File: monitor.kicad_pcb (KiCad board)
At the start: 4 copper layers, 35.5 x 33.7 mm, 51 parts, among them J1 USB_C_Plug, J2 USB_C_Receptacle_USB2.0_14P, J3 Display, J4 Program, J5 Boot, U1 STM32U031K8Ux, U2 TPSM365R6V3RDNR, U3 TMP117xxDRV, U4 REF5025ADGK, U5 CC6903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

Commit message: Footprint tweaks.
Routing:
- net GND: track 37.6 -> 42.0 mm
- net /DA-: track 30.2 -> 29.6 mm
- net /DA+: track 30.2 -> 29.6 mm

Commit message: Manufacturing updates
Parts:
- moved U2 0.55 mm to (113.3, 90.5)

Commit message: Robustify reset
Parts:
- added C20: 0u1, Capacitor_SMD:C_0402_1005Metric, F.Cu at (92.9, 108.6)
- added R19: 10k, Resistor_SMD:R_0603_1608Metric, B.Cu at (89.1, 114.0)
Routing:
- net /Vout: track 42.0 -> 50.0 mm, vias 6 -> 10
- net /VBus: track 32.9 -> 40.1 mm, vias 6 -> 8
- net GND: track 42.0 -> 44.8 mm, vias 43 -> 44
- net +3V3: track 237.2 -> 239.2 mm
- net Net-(J4-Pin_1): track 2.60 -> 4.60 mm

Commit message: Update monitor for actual display
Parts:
- removed R19: 10k, Resistor_SMD:R_0603_1608Metric
- H2: moved to B.Cu
- J3: footprint Parts:PinHeader_1x04_P2.54mm_Vertical -> Connector_JST:JST_EH_B4B-EH-A_1x04_P2.50mm_Vertical
- R1, R2, R7: footprint Resistor_SMD:R_0603_1608Metric -> Resistor_SMD:R_0402_1005Metric
- moved R13 8.36 mm to (101.2, 84.8)
- moved R1 8.04 mm to (98.6, 99.3), turned to 0 degrees
- moved C2 7.86 mm to (103.2, 96.6), turned to 90 degrees
- moved U5 4.52 mm to (99.9, 94.6), turned to -90 degrees
- moved R14 3.06 mm to (103.8, 84.8)
- moved R3 2.69 mm to (105.4, 91.6), turned to 0 degrees
- moved J3 2.53 mm to (96.2, 87.7), turned to 0 degrees
- moved R18 1.50 mm to (86.5, 92.2), turned to 180 degrees
- moved R17 1.26 mm to (86.5, 90.5), turned to 180 degrees
- moved D2 1.20 mm to (84.0, 92.2), turned to 0 degrees
- moved H1 1.00 mm to (84.2, 86.2)
- moved H2 1.00 mm to (115.8, 86.2), turned to 180 degrees
- moved D1 0.94 mm to (84.0, 90.5), turned to 0 degrees
- moved C9 0.32 mm to (96.0, 104.6)
- moved R2 0.30 mm to (98.6, 100.3)
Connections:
- J3 pad 1: +3V3 -> GND
- J3 pad 2: GND -> +3V3
- U5 pad 1: /Vout -> /VBus
- U5 pad 2: /Vout -> /VBus
- U5 pad 3: /VBus -> /Vout
- U5 pad 4: /VBus -> /Vout
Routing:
- net /VBus: track 40.1 -> 21.8 mm, vias 8 -> 0
- net /ISense: track 16.8 -> 7.74 mm
- net /VSense: track 13.8 -> 5.62 mm
- net /Vout: track 50.0 -> 46.6 mm
- net GND: track 44.8 -> 48.1 mm
- net /VBusFilt: track 7.13 -> 9.75 mm
- net /Red: track 26.2 -> 28.5 mm
- net Net-(J4-Pin_1): track 4.60 -> 2.60 mm
- net /PVcc: track 6.37 -> 5.16 mm, vias 2 -> 0
- net /SDA: track 40.4 -> 39.2 mm
- net Net-(D1-A): track 2.26 -> 1.20 mm
- net Net-(D2-A): track 2.21 -> 1.20 mm
- net +3V3: track 239.2 -> 239.9 mm, vias 13 -> 16
- net Earth: track 41.4 -> 40.8 mm
- removed copper zone on B.Cu, net /VBus

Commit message: Do a round of DRC and tidy-up.
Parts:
- moved R5 3.51 mm to (93.8, 84.8)
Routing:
- net /Alert: track 29.3 -> 30.0 mm

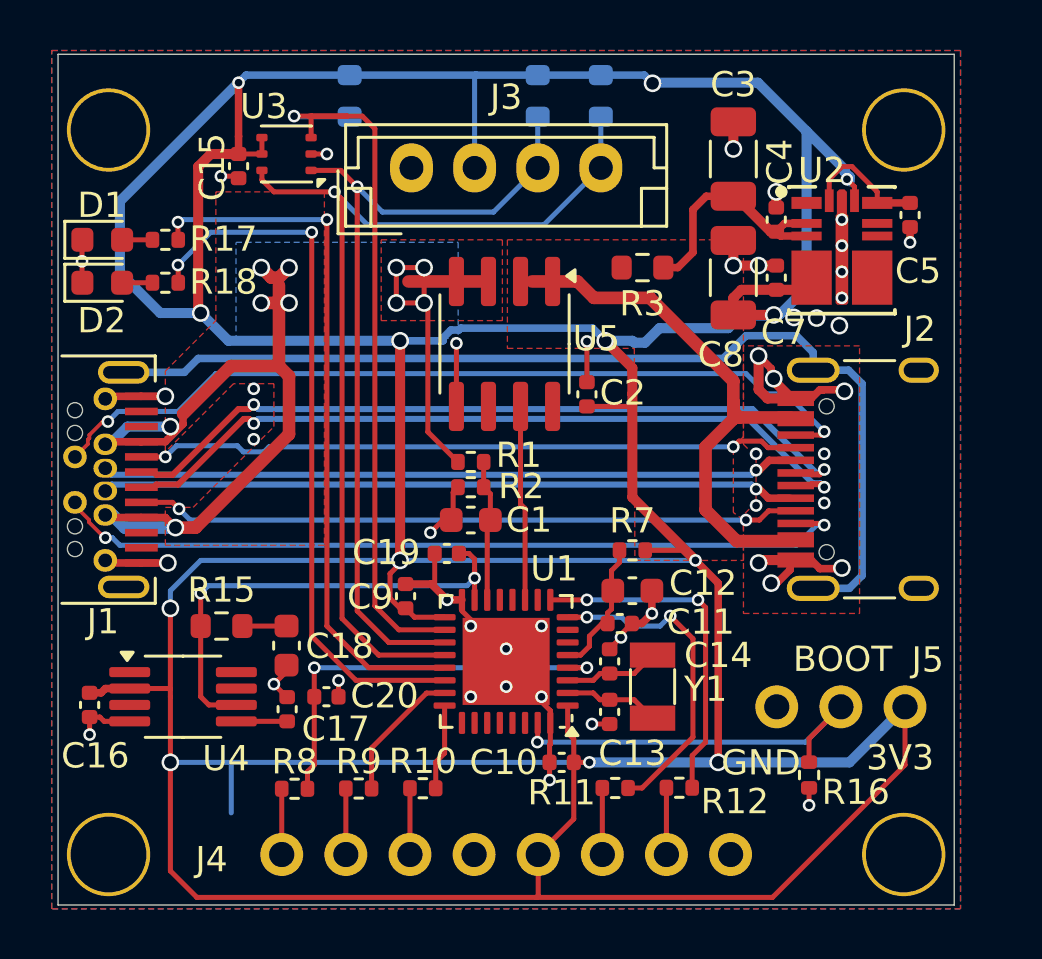
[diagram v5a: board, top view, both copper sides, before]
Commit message: Use a 2.54mm connector footprint.
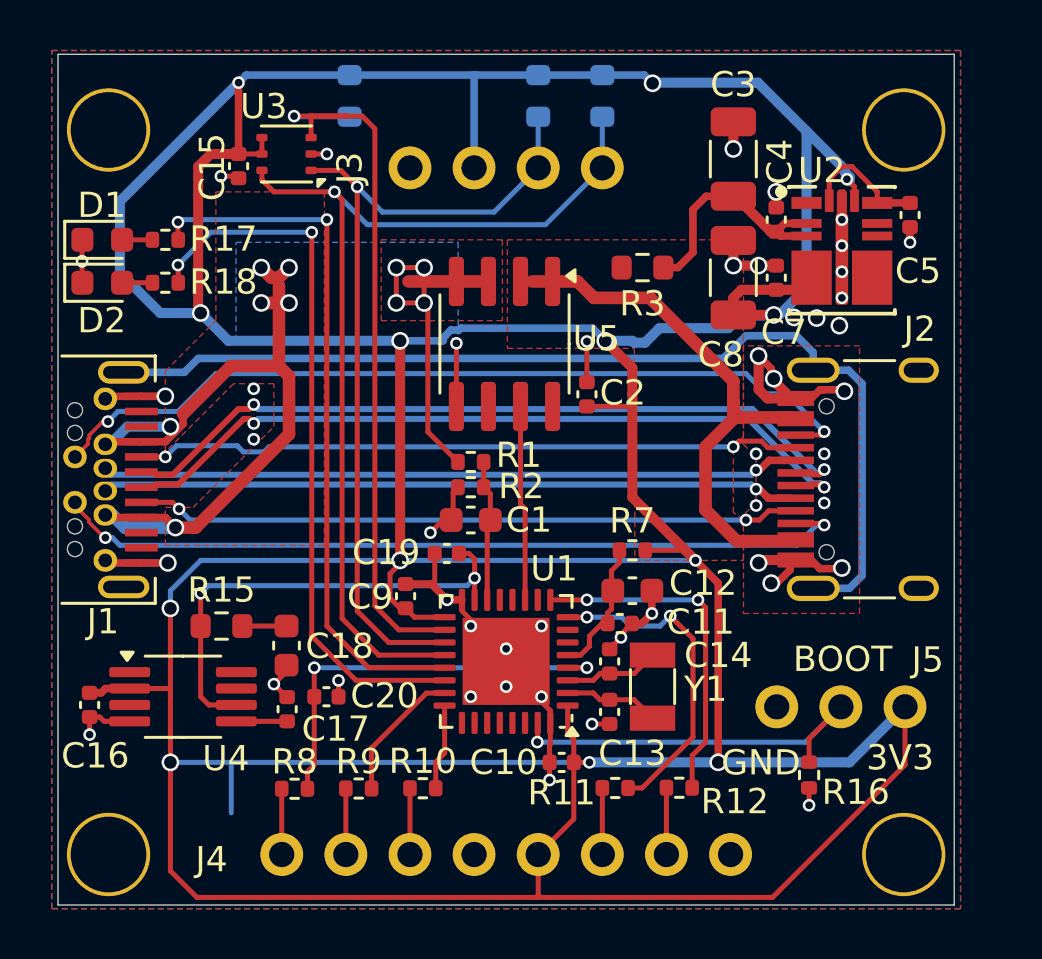
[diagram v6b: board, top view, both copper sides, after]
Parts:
- J3: footprint Connector_JST:JST_EH_B4B-EH-A_1x04_P2.50mm_Vertical -> Parts:PinHeader_1x04_P2.54mm_Vertical
- moved J3 0.06 mm to (96.2, 87.7), turned to 90 degrees
- moved R14 0.06 mm to (103.8, 84.8)

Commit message: Filter ADC input.
Tweak other capacitors.
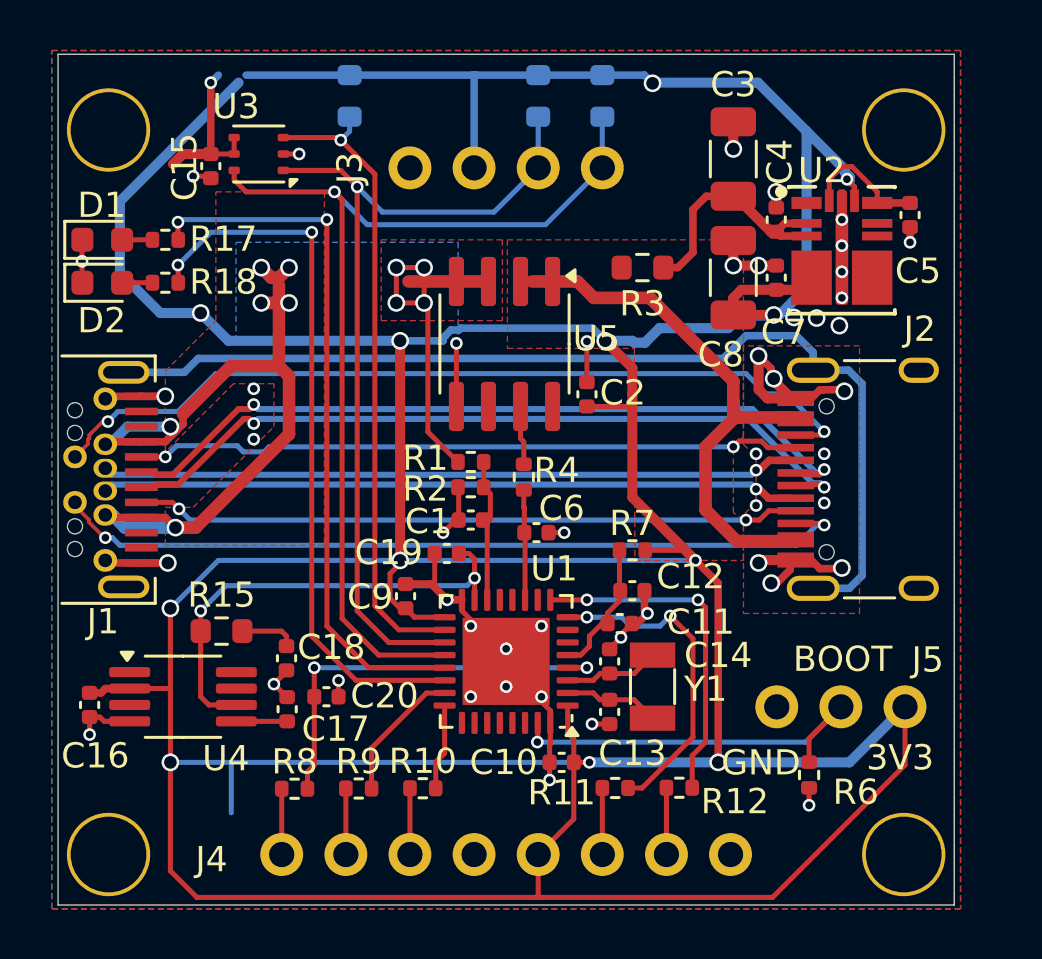
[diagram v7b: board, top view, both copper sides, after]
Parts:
- added C6: 10u, Capacitor_SMD:C_0402_1005Metric, F.Cu at (101.2, 102.1)
- added R4: 220, Resistor_SMD:R_0402_1005Metric, F.Cu at (100.7, 99.9)
- C1, C12, C18: value 22u -> 10u; footprint Capacitor_SMD:C_0603_1608Metric -> Capacitor_SMD:C_0402_1005Metric
- C16, C19: value 0u1 -> 1u
- moved C15 1.10 mm to (88.3, 87.6)
- moved U3 1.10 mm to (90.2, 87.1)
- moved C18 0.50 mm to (91.3, 107.1)
- moved R15 0.20 mm to (88.7, 106.0)
- renumbered R16 to R6
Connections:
- U5 pad 7: /ISense -> Net-(U5-VIOUT)
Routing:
- net +3V3: track 240.0 -> 233.6 mm
- net /Alert: track 30.0 -> 25.6 mm
- net /ISense: track 7.74 -> 4.33 mm
- net Net-(U5-VIOUT): track 0.00 -> 2.34 mm
- net /SCL: track 33.2 -> 34.3 mm
- net /SDA: track 39.2 -> 40.3 mm
- net GND: track 47.6 -> 48.1 mm, vias 44 -> 45

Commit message: Final updates.  Ordered.
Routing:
- net +3V3: track 233.6 -> 240.0 mm
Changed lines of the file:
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@@
 	)
 	(segment
+		(start 87.9 89.5)
+		(end 86.8 88.4)
+		(width 0.4)
+		(layer "F.Cu")
+		(net 3)
+	)
+	(segment
 		(start 107.5 103.2)
 		(end 108.4 104.1)
@@
 	)
 	(segment
+		(start 86.8 88.4)
+		(end 86.8 87.5)
+		(width 0.4)
+		(layer "F.Cu")
+		(net 3)
+	)
+	(segment
+		(start 86.8 87.5)
+		(end 87.2 87.1)
+		(width 0.4)
+		(layer "F.Cu")
+		(net 3)
+	)
+	(segment
 		(start 101.2 116.549)
 		(end 110.551 116.549)
@@
 	)
 	(segment
-		(start 86.8 87.5)
-		(end 87.2 87.1)
-		(width 0.4)
-		(layer "F.Cu")
-		(net 3)
-	)
-	(segment
 		(start 105 97.1)
 		(end 105 96.6)
@@
 	)
 	(segment
+		(start 87.2 87.1)
+		(end 88.3 87.1)
+		(width 0.4)
+		(layer "F.Cu")
+		(net 3)
+	)
+	(segment
 		(start 95.8 103.2)
 		(end 95.8 94.5)
@@
 	)
 	(segment
-		(start 87.2 87.1)
-		(end 88.3 87.1)
-		(width 0.4)
-		(layer "F.Cu")
-		(net 3)
-	)
-	(segment
 		(start 103.2 97.1)
 		(end 105 97.1)
@@
 	)
 	(segment
+		(start 87.9 93.4)
+		(end 87.9 89.5)
+		(width 0.4)
+		(layer "F.Cu")
+		(net 3)
+	)
+	(segment
 		(start 95.8 103.325)
 		(end 95.4 103.725)
@@
 	)
 	(zone
-		(net 65)
-		(net_name "/Vout")
-		(layer "F.Cu")
-		(name "$teardrop_padvia$")
-		(hatch none 0.1)
-		(priority 30003)
-		(attr
-			(teardrop
-				(type padvia)
-			)
-		)
-		(connect_pads yes
-			(clearance 0)
-		)
-		(min_thickness 0.0254)
-		(filled_areas_thickness no)
-		(fill yes
-			(thermal_gap 0.5)
-			(thermal_bridge_width 0.5)
-			(island_removal_mode 1)
-			(island_area_min 10)
-		)
-		(polygon
-			(pts
-				(xy 84.999756 101.65) (xy 84.999756 101.35) (xy 84.401117 101.046625) (xy 84.119 101.4) (xy 84.247913 101.816834)
-			)
-		)
-	)
-	(zone
 		(net 0)
 		(net_name "")
@@
 	)
 	(zone
-		(net 2)
-		(net_name "GND")
-		(layer "F.Cu")
-		(name "$teardrop_padvia$")
-		(hatch none 0.1)
-		(priority 30000)
-		(attr
-			(teardrop
-				(type padvia)
-			)
-		)
-		(connect_pads yes
-			(clearance 0)
-		)
-		(min_thickness 0.0254)
-		(filled_areas_thickness no)
-		(fill yes
-			(thermal_gap 0.5)
-			(thermal_bridge_width 0.5)
-			(island_removal_mode 1)
-			(island_area_min 10)
-		)
-		(polygon
-			(pts
-				(xy 85.026296 103.45) (xy 85.026296 103.15) (xy 84.390007 102.825839) (xy 84.119 103.2) (xy 84.227791 103.641353)
-			)
-		)
-	)
-	(zone
 		(net 65)
 		(net_name "/Vout")
@@
 	)
 	(zone
+		(net 65)
+		(net_name "/Vout")
+		(layer "F.Cu")
+		(name "$teardrop_padvia$")
+		(hatch none 0.1)
+		(priority 30002)
+		(attr
+			(teardrop
+				(type padvia)
+			)
+		)
+		(connect_pads yes
+			(clearance 0)
+		)
+		(min_thickness 0.0254)
+		(filled_areas_thickness no)
+		(fill yes
+			(thermal_gap 0.5)
+			(thermal_bridge_width 0.5)
+			(island_removal_mode 1)
+			(island_area_min 10)
+		)
+		(polygon
+			(pts
+				(xy 84.999756 98.65) (xy 84.999756 98.35) (xy 84.247913 98.183166) (xy 84.119 98.6) (xy 84.401117 98.953375)
+			)
+		)
+	)
+	(zone
 		(net 2)
 		(net_name "GND")
@@
 	)
 	(zone
+		(net 54)
+		(net_name "/SBU2")
+		(layer "F.Cu")
+		(name "$teardrop_padvia$")
+		(hatch none 0.1)
+		(priority 30004)
+		(attr
+			(teardrop
+				(type padvia)
+			)
+		)
+		(connect_pads yes
+			(clearance 0)
+		)
+		(min_thickness 0.0254)
+		(filled_areas_thickness no)
+		(fill yes
+			(thermal_gap 0.5)
+			(thermal_bridge_width 0.5)
+			(island_removal_mode 1)
+			(island_area_min 10)
+		)
+		(polygon
+			(pts
+				(xy 83.399851 101.606175) (xy 83.549851 101.606175) (xy 83.381353 100.812209) (xy 82.92 100.899)
+				(xy 82.649993 101.274161)
+			)
+		)
+	)
+	(zone
+		(net 65)
+		(net_name "/Vout")
+		(layer "F.Cu")
+		(name "$teardrop_padvia$")
+		(hatch none 0.1)
+		(priority 30003)
+		(attr
+			(teardrop
+				(type padvia)
+			)
+		)
+		(connect_pads yes
+			(clearance 0)
+		)
+		(min_thickness 0.0254)
+		(filled_areas_thickness no)
+		(fill yes
+			(thermal_gap 0.5)
+			(thermal_bridge_width 0.5)
+			(island_removal_mode 1)
+			(island_area_min 10)
+		)
+		(polygon
+			(pts
+				(xy 84.999756 101.65) (xy 84.999756 101.35) (xy 84.401117 101.046625) (xy 84.119 101.4) (xy 84.247913 101.816834)
+			)
+		)
+	)
+	(zone
 		(net 0)
 		(net_name "")
@@
 	)
 	(zone
-		(net 54)
-		(net_name "/SBU2")
+		(net 2)
+		(net_name "GND")
 		(layer "F.Cu")
 		(name "$teardrop_padvia$")
 		(hatch none 0.1)
-		(priority 30004)
+		(priority 30001)
 		(attr
 			(teardrop
@@
 		(polygon
 			(pts
-				(xy 83.399851 101.606175) (xy 83.549851 101.606175) (xy 83.381353 100.812209) (xy 82.92 100.899)
-				(xy 82.649993 101.274161)
+				(xy 85.026296 96.85) (xy 85.026296 96.55) (xy 84.227791 96.358647) (xy 84.119 96.8) (xy 84.390007 97.174161)
 			)
 		)
 	)
 	(zone
-		(net 2)
-		(net_name "GND")
+		(net 65)
+		(net_name "/Vout")
 		(layer "F.Cu")
-		(name "$teardrop_padvia$")
-		(hatch none 0.1)
-		(priority 30001)
-		(attr
-			(teardrop
-				(type padvia)
-			)
-		)
-		(connect_pads yes
-			(clearance 0)
+		(name "Vout")
+		(hatch edge 0.5)
+		(priority 10)
+		(connect_pads
+			(clearance 0.15)
 		)
-		(min_thickness 0.0254)
+		(min_thickness 0.15)
 		(filled_areas_thickness no)
 		(fill yes
-			(thermal_gap 0.5)
-			(thermal_bridge_width 0.5)
-			(island_removal_mode 1)
-			(island_area_min 10)
+			(thermal_gap 0.15)
+			(thermal_bridge_width 0.25)
 		)
 		(polygon
 			(pts
-				(xy 85.026296 96.85) (xy 85.026296 96.55) (xy 84.227791 96.358647) (xy 84.119 96.8) (xy 84.390007 97.174161)
+				(xy 92.8 88.6) (xy 92.8 102.6) (xy 86.5 102.6) (xy 86.5 101.1) (xy 87.6 101.1) (xy 90.8 97.9015)
+				(xy 90.8 96.2) (xy 89.2 96.2) (xy 86.5 98.9) (xy 86.5 95.7) (xy 88.5 93.7) (xy 88.5 88.6)
 			)
 		)
 	)
 	(zone
-		(net 65)
-		(net_name "/Vout")
+		(net 20)
+		(net_name "/CC2")
 		(layer "F.Cu")
 		(name "$teardrop_padvia$")
 		(hatch none 0.1)
-		(priority 30002)
+		(priority 30005)
 		(attr
 			(teardrop
@@
 		(polygon
 			(pts
-				(xy 84.999756 98.65) (xy 84.999756 98.35) (xy 84.247913 98.183166) (xy 84.119 98.6) (xy 84.401117 98.953375)
-			)
-		)
-	)
-	(zone
-		(net 65)
-		(net_name "/Vout")
-		(layer "F.Cu")
-		(name "Vout")
-		(hatch edge 0.5)
-		(priority 10)
-		(connect_pads
-			(clearance 0.15)
-		)
-		(min_thickness 0.15)
-		(filled_areas_thickness no)
-		(fill yes
-			(thermal_gap 0.15)
-			(thermal_bridge_width 0.25)
-		)
-		(polygon
-			(pts
-				(xy 92.8 88.6) (xy 92.8 102.6) (xy 86.5 102.6) (xy 86.5 101.1) (xy 87.6 101.1) (xy 90.8 97.9015)
-				(xy 90.8 96.2) (xy 89.2 96.2) (xy 86.5 98.9) (xy 86.5 95.7) (xy 88.5 93.7) (xy 88.5 88.6)
+				(xy 83.505 98.42) (xy 83.355 98.42) (xy 82.649993 98.725839) (xy 82.92 99.101) (xy 83.381353 99.187791)
 			)
 		)
 	)
 	(zone
-		(net 20)
-		(net_name "/CC2")
+		(net 2)
+		(net_name "GND")
 		(layer "F.Cu")
 		(name "$teardrop_padvia$")
 		(hatch none 0.1)
-		(priority 30005)
+		(priority 30000)
 		(attr
 			(teardrop
@@
 		(polygon
 			(pts
-				(xy 83.505 98.42) (xy 83.355 98.42) (xy 82.649993 98.725839) (xy 82.92 99.101) (xy 83.381353 99.187791)
+				(xy 85.026296 103.45) (xy 85.026296 103.15) (xy 84.390007 102.825839) (xy 84.119 103.2) (xy 84.227791 103.641353)
 			)
 		)
@@
 		(net_name "/Vout")
 		(layer "B.Cu")
+		(name "VoutB")
+		(hatch edge 0.5)
+		(priority 10)
+		(connect_pads
+			(clearance 0.15)
+		)
+		(min_thickness 0.3)
+		(filled_areas_thickness no)
+		(fill yes
+			(thermal_gap 0.15)
+			(thermal_bridge_width 0.25)
+		)
+		(polygon
+			(pts
+				(xy 89.3 90.6) (xy 98.1 90.6) (xy 98.1 94.4) (xy 89.3 94.508642)
+			)
+		)
+	)
+	(zone
+		(net 65)
+		(net_name "/Vout")
+		(layer "B.Cu")
 		(name "$teardrop_padvia$")
 		(hatch none 0.1)
-		(priority 30001)
+		(priority 30000)
 		(attr
 			(teardrop
@@
 		(polygon
 			(pts
-				(xy 84.965513 98.217329) (xy 84.682671 97.934487) (xy 83.992087 98.183166) (xy 84.119293 98.600707)
-				(xy 84.519987 98.832224)
-			)
-		)
-	)
-	(zone
-		(net 65)
-		(net_name "/Vout")
-		(layer "B.Cu")
-		(name "VoutB")
-		(hatch edge 0.5)
-		(priority 10)
-		(connect_pads
-			(clearance 0.15)
-		)
-		(min_thickness 0.3)
-		(filled_areas_thickness no)
-		(fill yes
-			(thermal_gap 0.15)
-			(thermal_bridge_width 0.25)
-		)
-		(polygon
-			(pts
-				(xy 89.3 90.6) (xy 98.1 90.6) (xy 98.1 94.4) (xy 89.3 94.508642)
+				(xy 84.676604 102.030158) (xy 85.030158 101.676604) (xy 84.518375 101.163883) (xy 84.119293 101.399293)
+				(xy 83.992087 101.816834)
 			)
 		)
@@
 		(name "$teardrop_padvia$")
 		(hatch none 0.1)
-		(priority 30000)
+		(priority 30001)
 		(attr
 			(teardrop
@@
 		(polygon
 			(pts
-				(xy 84.676604 102.030158) (xy 85.030158 101.676604) (xy 84.518375 101.163883) (xy 84.119293 101.399293)
-				(xy 83.992087 101.816834)
+				(xy 84.965513 98.217329) (xy 84.682671 97.934487) (xy 83.992087 98.183166) (xy 84.119293 98.600707)
+				(xy 84.519987 98.832224)
 			)
 		)
